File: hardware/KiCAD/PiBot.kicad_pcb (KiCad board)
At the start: 2 copper layers, 149 parts, among them P1 BREAKOUT, P10 BREAKOUT, P11 BREAKOUT, P12 BREAKOUT, P2 CONN_02X05, P3 I2C_EXPANSION, P4 SPI_EXPANSION, P6 BREAKOUT, P7 BREAKOUT, P8 BREAKOUT, P9 BREAKOUT, U1 DMG2302U, U10 AH3772, U11 AH3772, U12 AH3772, U3 DMG2302U, U9 AH3772

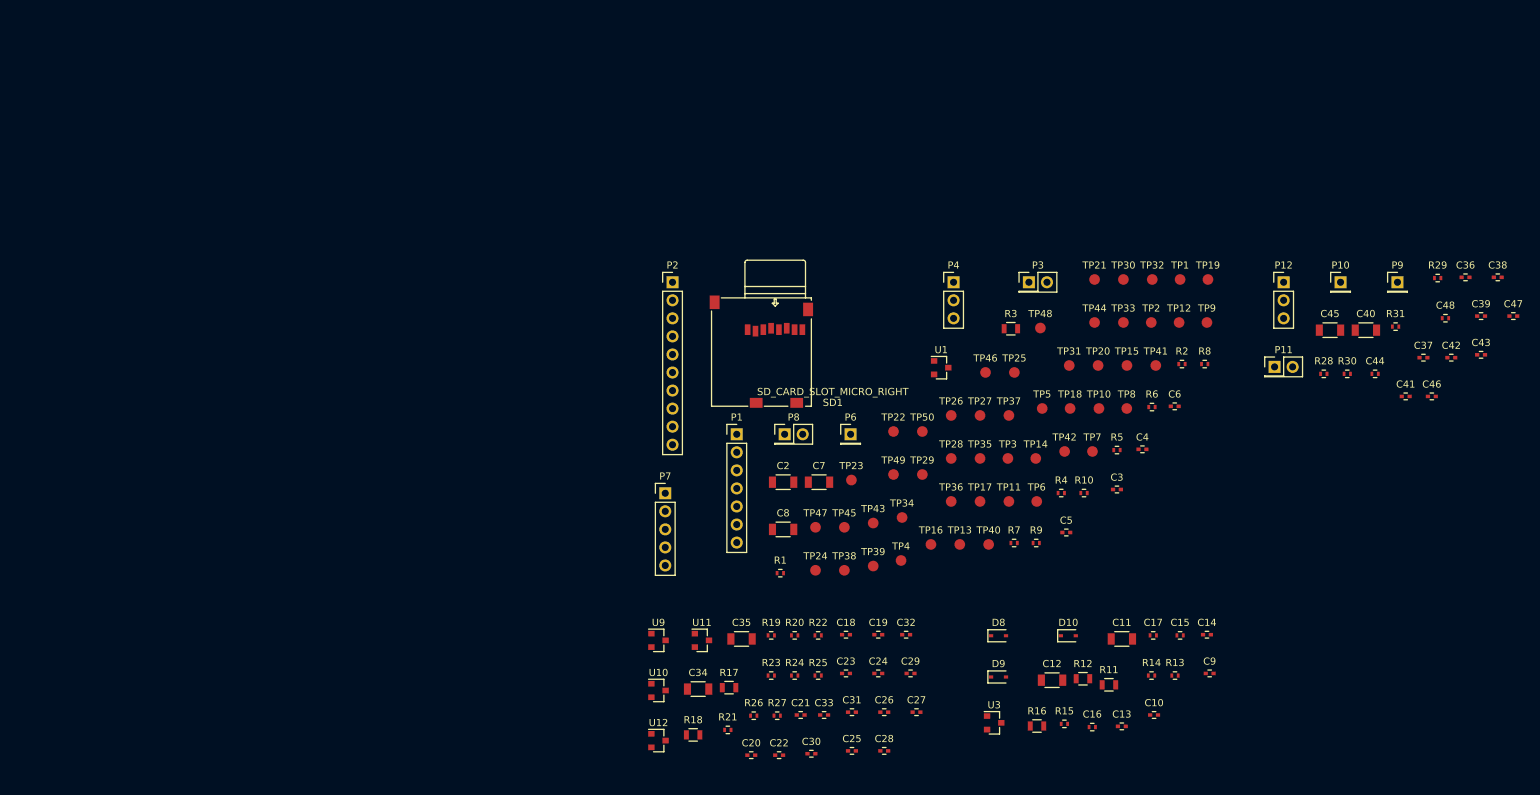
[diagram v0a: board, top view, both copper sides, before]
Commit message: Add the rest of the missing footprints, aside from motor
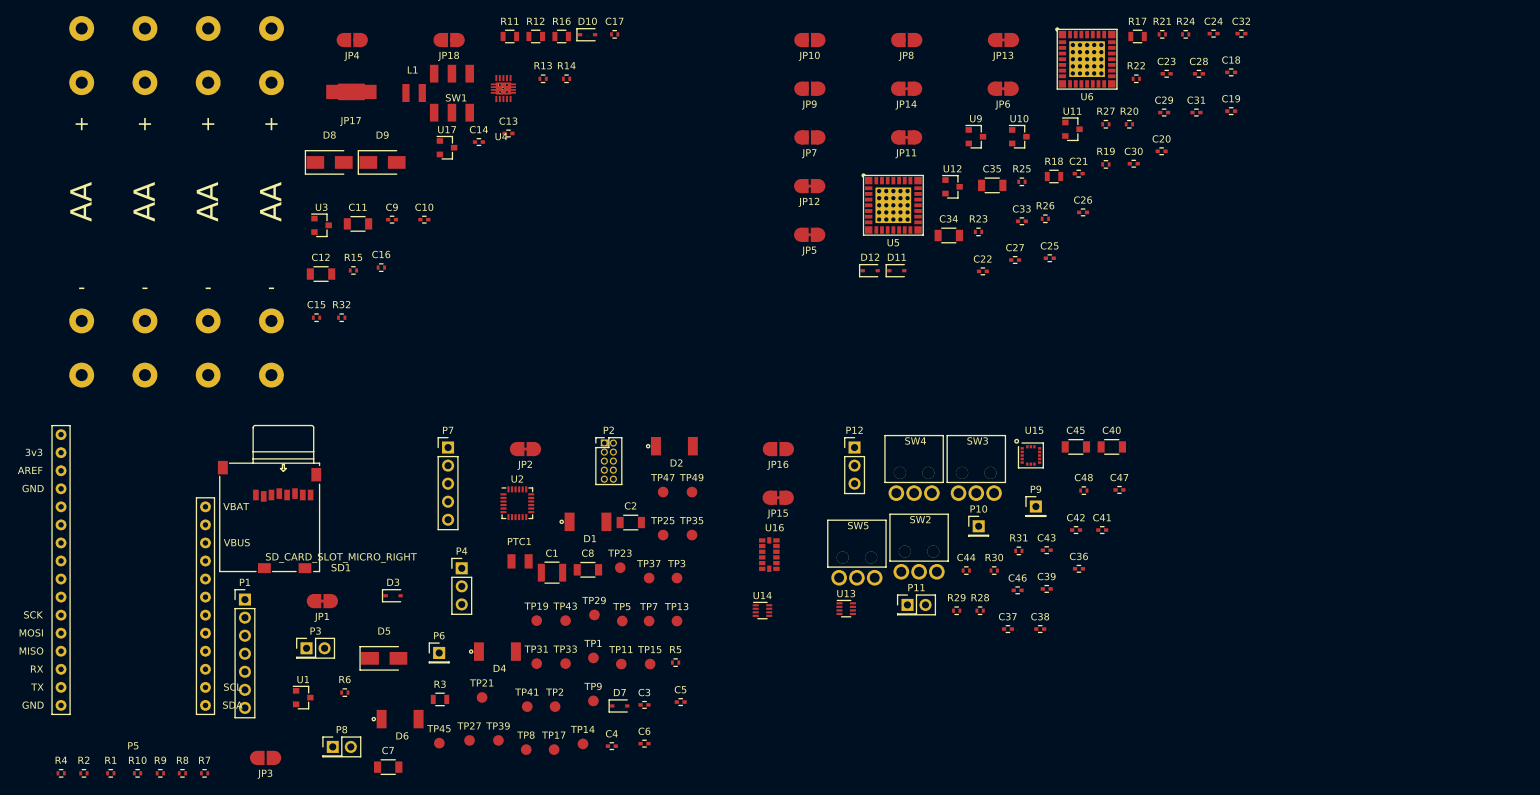
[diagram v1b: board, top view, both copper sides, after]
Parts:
- removed TP10, TP12, TP16, TP18, TP20, TP22, TP24, TP26, TP28, TP30, TP32, TP34, TP36, TP38, TP4, TP40, TP42, TP44, TP46, TP48, TP50, TP6: TEST, Measurement_Points:Measurement_Point_Round-SMD-Pad_Small
- added BT1: Battery, PiBot:AA_Batt, F.Cu at (75.6, 83.5)
- added BT2: Battery, PiBot:AA_Batt, F.Cu at (84.5, 83.5)
- added BT3: Battery, PiBot:AA_Batt, F.Cu at (93.4, 83.5)
- added BT4: Battery, PiBot:AA_Batt, F.Cu at (102.3, 83.5)
- added C1: 100uF, Capacitors_SMD:C_1210, F.Cu at (141.7, 135.7)
- added D1: LED, PiBot:PLCC2-LED-Reverse, F.Cu at (146.8, 128.5)
- added D11: 3.3V, Diodes_SMD:SOD-323, F.Cu at (190.3, 93.2)
- added D12: 3.3V, Diodes_SMD:SOD-323, F.Cu at (186.5, 93.2)
- added D2: LED, PiBot:PLCC2-LED-Reverse, F.Cu at (159.0, 117.9)
- added D3: Schottky, Diodes_SMD:SOD-323, F.Cu at (119.4, 138.9)
- added D4: LED, PiBot:PLCC2-LED-Reverse, F.Cu at (134.1, 146.8)
- added D5: 5.1V, Diodes_SMD:SMA_Standard, F.Cu at (118.1, 147.7)
- added D6: LED, PiBot:PLCC2-LED-Reverse, F.Cu at (120.4, 156.3)
- added D7: 3.3V, Diodes_SMD:SOD-323, F.Cu at (151.3, 154.4)
- added JP1: Jumper_NC_Small, PiBot:Jumper-NC, F.Cu at (109.4, 139.7)
- added JP10: Jumper_NO_Small, PiBot:Jumper-NO, F.Cu at (178.0, 60.7)
- added JP11: Jumper_NC_Small, PiBot:Jumper-NC, F.Cu at (191.6, 74.4)
- added JP12: Jumper_NC_Small, PiBot:Jumper-NC, F.Cu at (178.0, 81.3)
- added JP13: Jumper_NC_Small, PiBot:Jumper-NC, F.Cu at (205.3, 60.7)
- added JP14: Jumper_NC_Small, PiBot:Jumper-NC, F.Cu at (191.6, 67.6)
- added JP15: Jumper_NC_Small, PiBot:Jumper-NC, F.Cu at (173.6, 125.1)
- added JP16: Jumper_NO_Small, PiBot:Jumper-NO, F.Cu at (173.6, 118.3)
- added JP17: Jumper_NC_Small, Oddities:NetTie-I_Connected_SMD, F.Cu at (113.5, 68.0)
- added JP18: Jumper_NO_Small, PiBot:Jumper-NO, F.Cu at (127.3, 60.7)
- added JP2: Jumper_NC_Small, PiBot:Jumper-NC, F.Cu at (138.0, 118.3)
- added JP3: Jumper_NO_Small, PiBot:Jumper-NO, F.Cu at (101.4, 161.7)
- added JP4: Jumper_NO_Small, PiBot:Jumper-NO, F.Cu at (113.6, 60.7)
- added JP5: Jumper_NC_Small, PiBot:Jumper-NC, F.Cu at (178.0, 88.1)
- added JP6: Jumper_NC_Small, PiBot:Jumper-NC, F.Cu at (205.2, 67.6)
- added JP7: Jumper_NO_Small, PiBot:Jumper-NO, F.Cu at (178.0, 74.4)
- added JP8: Jumper_NO_Small, PiBot:Jumper-NO, F.Cu at (191.7, 60.7)
- added JP9: Jumper_NO_Small, PiBot:Jumper-NO, F.Cu at (178.0, 67.6)
- added L1: 1 uH, Inductors_NEOSID:Neosid_Inductor_SM-NE29_SMD1008, F.Cu at (122.3, 68.2)
- added P5: Feather-Adaper, PiBot:feather-headers, F.Cu at (82.8, 141.6)
- added PTC1: 0.5A, Fuse_Holders_and_Fuses:Fuse_SMD1206_Reflow, F.Cu at (137.2, 134.1)
- added R32: 10k, Resistors_SMD:R_0402, F.Cu at (112.2, 99.8)
- added SW1: SPST, PiBot:JS202011SCQN, F.Cu at (127.7, 68.2)
- added SW2: SW_SPDT, PiBot:TS0101F020V3, F.Cu at (193.4, 135.5)
- added SW3: SW_SPDT, PiBot:TS0101F020V3, F.Cu at (201.4, 124.5)
- added SW4: SW_SPDT, PiBot:TS0101F020V3, F.Cu at (192.7, 124.5)
- added SW5: SW_SPDT, PiBot:TS0101F020V3, F.Cu at (184.6, 136.4)
- added U13: BH1745NUC, Housings_DFN_QFN:DFN-8_2x2mm_Pitch0.5mm, F.Cu at (183.1, 140.7)
- added U14: BH1745NUC, Housings_DFN_QFN:DFN-8_2x2mm_Pitch0.5mm, F.Cu at (171.4, 141.0)
- added U15: L3GD20H, PiBot:16-LGA-3x3, F.Cu at (209.1, 119.2)
- added U16: LSM303DLHCTR, PiBot:14-LGA-3x5, F.Cu at (172.3, 133.1)
- added U17: N-FET, TO_SOT_Packages_SMD:SOT-23, F.Cu at (127.0, 75.9)
- added U2: MKL03ZxxVFK4, Housings_DFN_QFN:QFN-24_4x4mm_Pitch0.5mm, F.Cu at (136.9, 125.9)
- added U4: TPS63060, PiBot:DFN-10-w_pad, F.Cu at (134.9, 67.5)
- added U5: MC33926PNB, PiBot:PQFN-32-EP-0.8mm, F.Cu at (189.8, 84.0)
- added U6: MC33926PNB, PiBot:PQFN-32-EP-0.8mm, F.Cu at (217.0, 63.4)
- D10: value DZ2J075M0L -> 7.5V
- D8, D9: value DZ2J051M0L -> 5.1V; footprint Diodes_SMD:SOD-323 -> Diodes_SMD:SMA_Standard
- P2: footprint Pin_Headers:Pin_Header_Straight_1x10_Pitch2.54mm -> Pin_Headers:Pin_Header_Straight_2x05_Pitch1.27mm
- U3: value DMG2302U -> N-FET
- moved R2 164.9 mm to (75.9, 163.9)
- moved R8 154.9 mm to (89.7, 163.9)
- moved R4 146.1 mm to (72.7, 163.9)
- moved R10 138.9 mm to (83.4, 163.9)
- moved C9 131.6 mm to (119.2, 86.0)
- moved C15 129.5 mm to (108.6, 99.8)
- moved R9 127.4 mm to (86.6, 163.9)
- moved R11 124.2 mm to (135.8, 60.2)
- moved C10 124.1 mm to (123.8, 86.0)
- moved C14 123.7 mm to (131.5, 75.1)
- moved C11 122.3 mm to (114.4, 86.6)
- moved R13 122.3 mm to (140.5, 66.2)
- moved R6 120.5 mm to (112.6, 152.5)
- moved C13 120.0 mm to (135.6, 73.9)
- moved C16 119.1 mm to (117.7, 92.7)
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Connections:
- net /power/+BATT_ISOLATED renamed /power/BATT_V+_TERM
- C28 pad 2: GND -> GNDPWR
- C29 pad 2: GND -> GNDPWR
- C32 pad 2: GND -> GNDPWR
- C33 pad 2: GND -> GNDPWR
- C34 pad 2: GND -> GNDPWR
- C35 pad 2: GND -> GNDPWR
- C9 pad 2: /power/BATT_GND_TERM -> Net-(C9-Pad2)
- U3 pad 3: /power/BATT_GND_TERM -> Net-(C9-Pad2)

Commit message: Started board layout
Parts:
- moved R10 193.2 mm to (232.2, 40.6), turned to 90 degrees
- moved R9 191.9 mm to (232.2, 38.7), turned to 90 degrees
- moved JP3 173.1 mm to (219.5, 35.1), turned to 90 degrees
- moved C7 160.5 mm to (220.7, 39.1)
- moved D7 141.1 mm to (233.8, 40.0), turned to 270 degrees
- moved C4 138.9 mm to (222.4, 41.4), turned to 270 degrees
- moved C6 135.0 mm to (219.8, 41.4), turned to 270 degrees
- moved C8 131.0 mm to (236.0, 39.2), turned to 270 degrees
- moved C5 128.1 mm to (221.1, 41.4), turned to 270 degrees
- moved U2 124.6 mm to (226.8, 39.8)
- moved R8 119.0 mm to (195.8, 109.9)
- moved R4 119.0 mm to (178.7, 109.9)
- moved R7 119.0 mm to (198.9, 109.9)
- moved JP2 118.4 mm to (219.5, 32.4), turned to 270 degrees
- moved R29 118.0 mm to (174.1, 25.7)
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
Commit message: Dry positioning of large portion of the components
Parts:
- added U7: Motor, PiBot:Sanyo_GearMotor, F.Cu at (111.0, 110.0)
- added U8: Motor, PiBot:Sanyo_GearMotor, F.Cu at (175.0, 110.0)
- C1, C10, C11, C12, C13, C14, C15, C16, C17, C2, C20, C21, C3, C38, C9, D1, D10, D11, D12, D2, D4, D6, D8, D9, JP10, JP11, JP12, JP13, JP14, JP17, JP18, JP4, JP5, JP6, JP7, JP8, JP9, L1, R1, R11, R12, R13, R14, R15, R16, R17, R18, R19, R2, R20, R28, R3, R30, R32, R6, SD1, SW2, SW3, U1, U17, U3, U4: moved to B.Cu
- moved R11 195.3 mm to (229.2, 145.2), turned to 0 degrees
- moved L1 189.5 mm to (233.5, 148.0)
- moved R32 189.0 mm to (221.0, 145.5)
- moved C17 187.9 mm to (240.0, 147.5), turned to 270 degrees
- moved C16 187.5 mm to (238.5, 147.5), turned to 270 degrees
- moved D8 187.3 mm to (216.8, 140.8)
- moved C15 187.1 mm to (237.0, 147.5), turned to 270 degrees
- moved JP18 185.9 mm to (220.5, 148.0)
- moved U4 184.9 mm to (233.5, 144.0), turned to 90 degrees
- moved U17 184.7 mm to (221.0, 142.5), turned to 90 degrees
- moved R15 184.6 mm to (239.5, 140.8), turned to 0 degrees
- moved R14 183.6 mm to (237.2, 140.5)
- moved C9 183.0 mm to (228.2, 142.5), turned to 90 degrees
- moved R16 182.9 mm to (238.0, 144.5), turned to 0 degrees
- moved C14 182.9 mm to (237.5, 142.5), turned to 0 degrees
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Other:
- board outline added: 112 x 87 mm

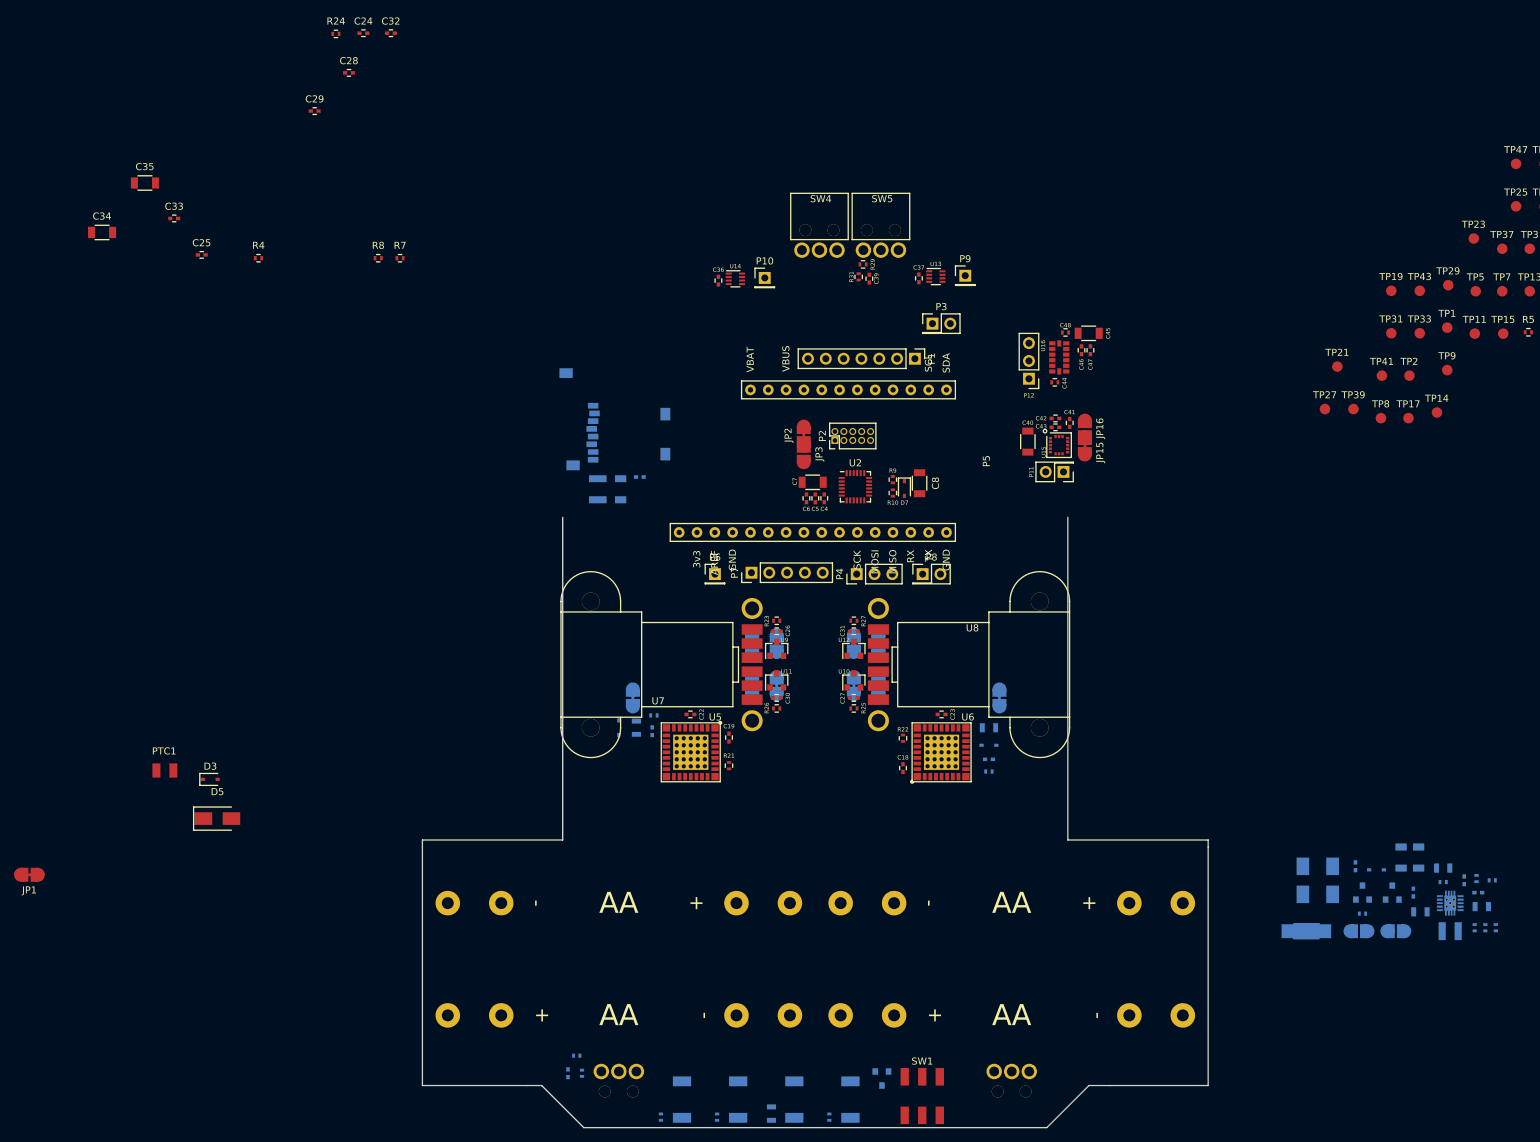
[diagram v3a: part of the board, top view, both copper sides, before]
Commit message: Initial laying of traces, still work to get done
batt_v+_term trace is way too thing right now
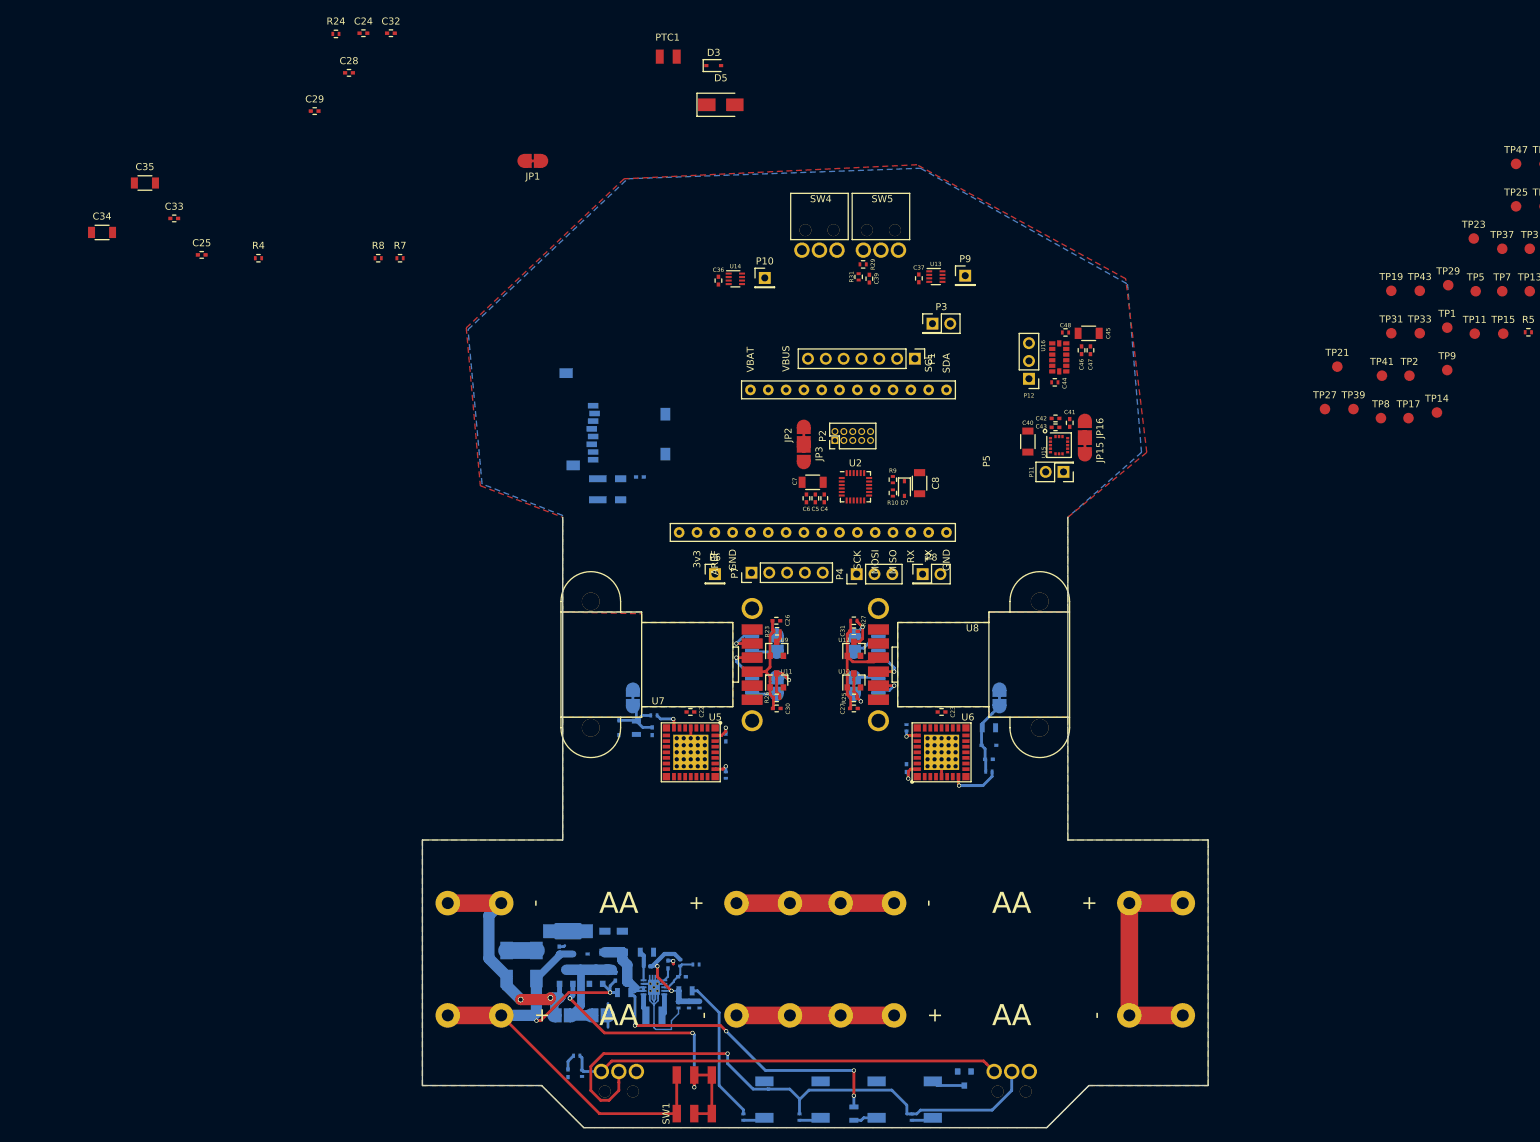
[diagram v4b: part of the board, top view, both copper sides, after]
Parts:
- C18, C19, R21, R22: moved to B.Cu
- moved D3 124.5 mm to (128.5, 24.6)
- moved D5 124.5 mm to (129.5, 30.2)
- moved JP1 124.5 mm to (102.7, 38.2)
- moved PTC1 124.5 mm to (122.0, 23.3)
- moved C9 114.4 mm to (114.5, 154.5)
- moved C10 114.1 mm to (106.5, 150.8)
- moved C11 114.1 mm to (113.0, 149.5)
- moved C12 114.1 mm to (115.5, 149.5)
- moved C13 114.1 mm to (122.0, 152.8)
- moved C14 114.1 mm to (124.0, 154.5)
- moved D10 114.1 mm to (109.5, 151.2)
- moved D8 114.1 mm to (103.2, 152.8)
- moved D9 114.1 mm to (99.0, 152.8)
- moved JP18 114.1 mm to (107.0, 160.0)
- moved JP4 114.1 mm to (112.2, 160.0), turned to 0 degrees
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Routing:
- net +3V3: track 0.00 -> 119.3 mm, vias 0 -> 1
- net /power/BATT_V+_TERM: track 0.00 -> 78.8 mm, vias 0 -> 2
- net Net-(R28-Pad1): track 0.00 -> 62.2 mm
- net +BATT: track 0.00 -> 57.2 mm, vias 0 -> 4
- net Net-(R32-Pad1): track 0.00 -> 41.9 mm, vias 0 -> 3
- net /power/BATT_GND_TERM: track 0.00 -> 34.8 mm, vias 0 -> 2
- net Net-(BT2-Pad2): track 0.00 -> 31.2 mm
- net GND: track 0.00 -> 25.9 mm, vias 0 -> 1
- net Net-(BT3-Pad2): track 0.00 -> 22.5 mm
- net Net-(BT1-Pad2): track 0.00 -> 22.5 mm
- net +5V: track 0.00 -> 21.0 mm
- net /power/PSU_VOUT: track 0.00 -> 18.1 mm, vias 0 -> 2
- net Net-(C9-Pad2): track 0.00 -> 17.5 mm
- net Net-(C21-Pad1): track 0.00 -> 10.6 mm
- net Net-(R20-Pad1): track 0.00 -> 10.5 mm, vias 0 -> 1
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- added copper zone on B.Cu, net GND
- added copper zone on F.Cu, net GND
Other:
- net class Default: trace_width 0.25 -> 0.4
- board text added: "3v"
- board text added: "5v"
- board text added: "B+"
- board text added: "MC"
